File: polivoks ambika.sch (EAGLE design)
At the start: 69 parts, among them IC1 TL084, IC10 LM4250P, IC11 LM13700N, IC2 4052N, IC5 TL072, IC6 MCP4822, IC7 ATMega328p, IC9 LM4250P, Q1 2N3906, Q2 2N3906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

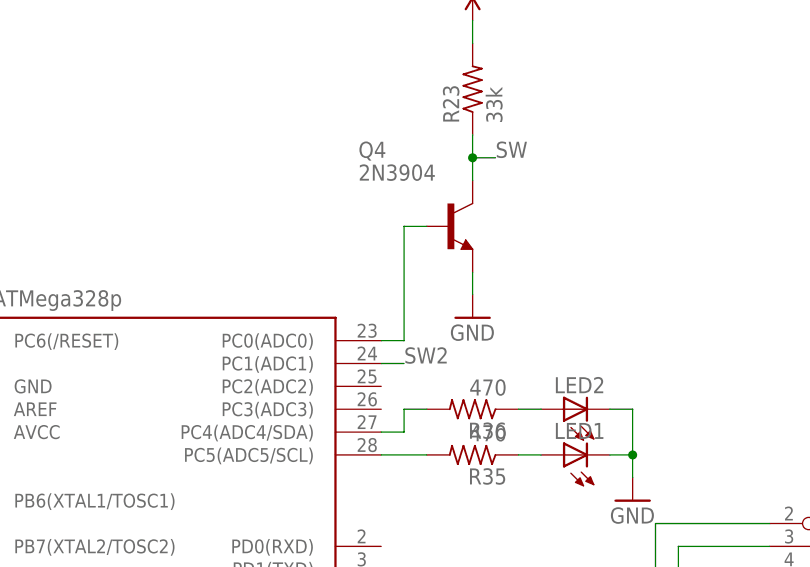
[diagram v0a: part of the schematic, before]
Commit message: Added a resistor to limit the current on BP mode
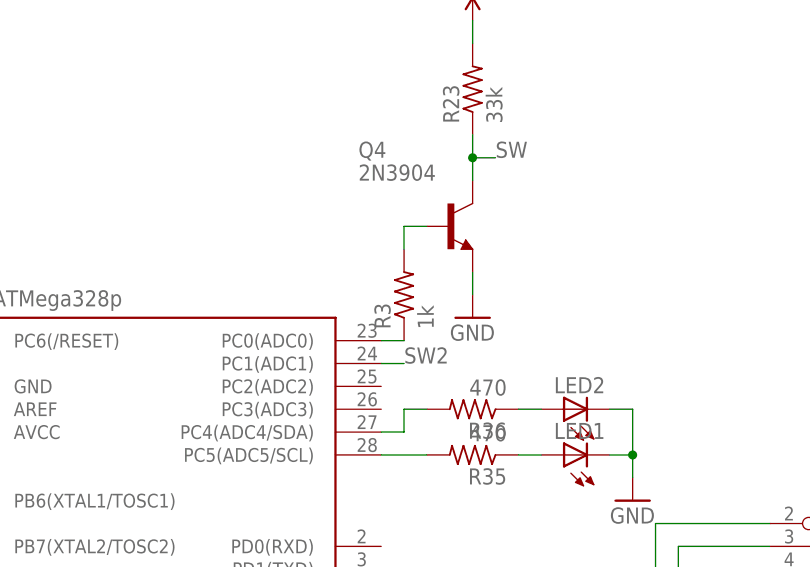
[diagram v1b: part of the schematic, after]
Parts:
- added R3: 1k, rcl:R-US_0204/7
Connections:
- new net N$23: IC7.PC0(ADC0), R3.1
- net N$21: now also R3.2; no longer IC7.PC0(ADC0)
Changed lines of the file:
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@@
 <part name="C17" library="rcl" deviceset="C-US" device="025-025X050" value="100n"/>
 <part name="GND8" library="SparkFun" deviceset="GND" device=""/>
+<part name="R3" library="rcl" deviceset="R-US_" device="0204/7" value="1k"/>
 </parts>
 <sheets>
@@
 <instance part="IC11" gate="SUPPLY" x="261.62" y="137.16"/>
 <instance part="GND8" gate="1" x="210.82" y="-35.56"/>
+<instance part="R3" gate="G$1" x="71.12" y="96.52" rot="R90"/>
 </instances>
 <busses>
@@
 <wire x1="71.12" y1="104.14" x2="73.66" y2="104.14" width="0.1524" layer="91"/>
 <pinref part="Q4" gate="G1" pin="B"/>
-<wire x1="71.12" y1="104.14" x2="71.12" y2="91.44" width="0.1524" layer="91"/>
-<pinref part="IC7" gate="G$1" pin="PC0(ADC0)"/>
-<wire x1="71.12" y1="91.44" x2="68.58" y2="91.44" width="0.1524" layer="91"/>
+<pinref part="R3" gate="G$1" pin="2"/>
+<wire x1="71.12" y1="101.6" x2="71.12" y2="104.14" width="0.1524" layer="91"/>
 </segment>
 </net>
@@
 </segment>
 </net>
+<net name="N$23" class="0">
+<segment>
+<pinref part="IC7" gate="G$1" pin="PC0(ADC0)"/>
+<wire x1="71.12" y1="91.44" x2="68.58" y2="91.44" width="0.1524" layer="91"/>
+<pinref part="R3" gate="G$1" pin="1"/>
+</segment>
+</net>
